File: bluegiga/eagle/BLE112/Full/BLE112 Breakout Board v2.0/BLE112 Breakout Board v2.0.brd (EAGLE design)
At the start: 38.1 x 22.9 mm, 27 parts, among them U1 BLE112-A, U2 MCP1700

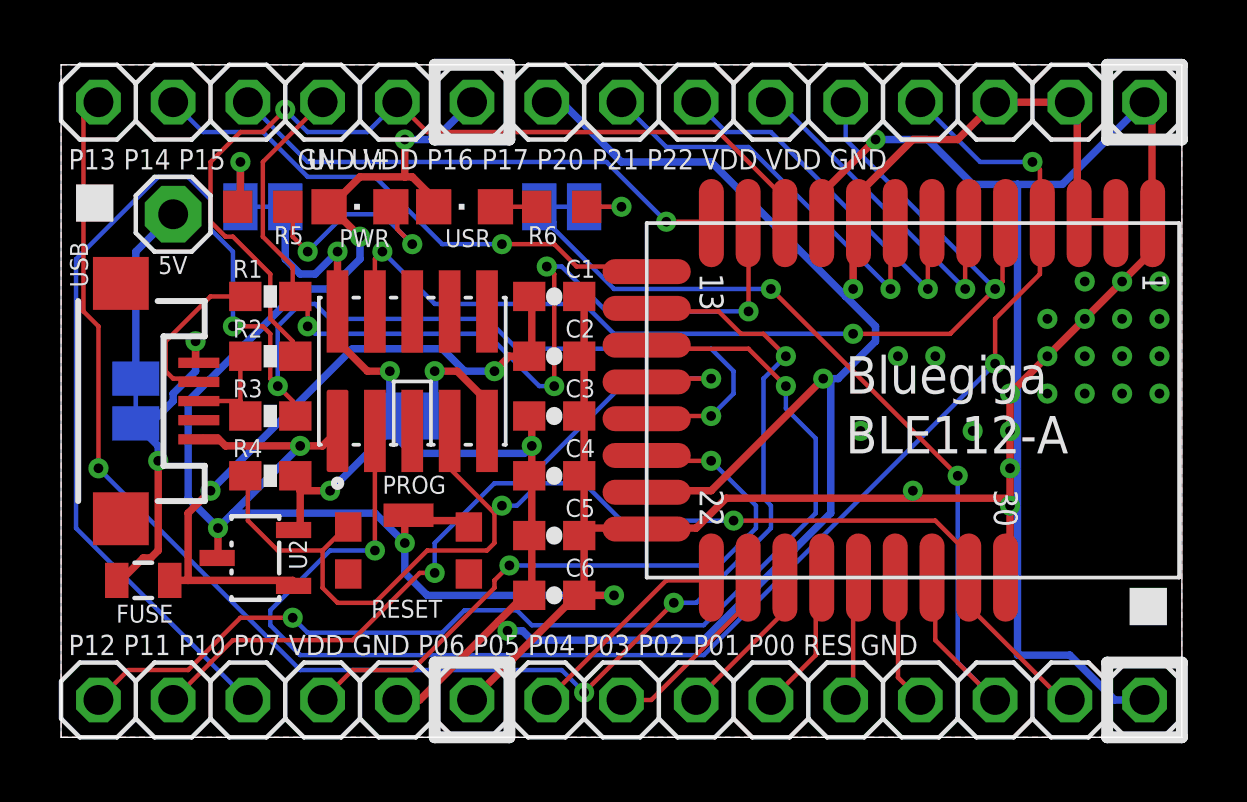
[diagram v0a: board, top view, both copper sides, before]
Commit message: Fix BLE112 v2.0 trial run PCB error
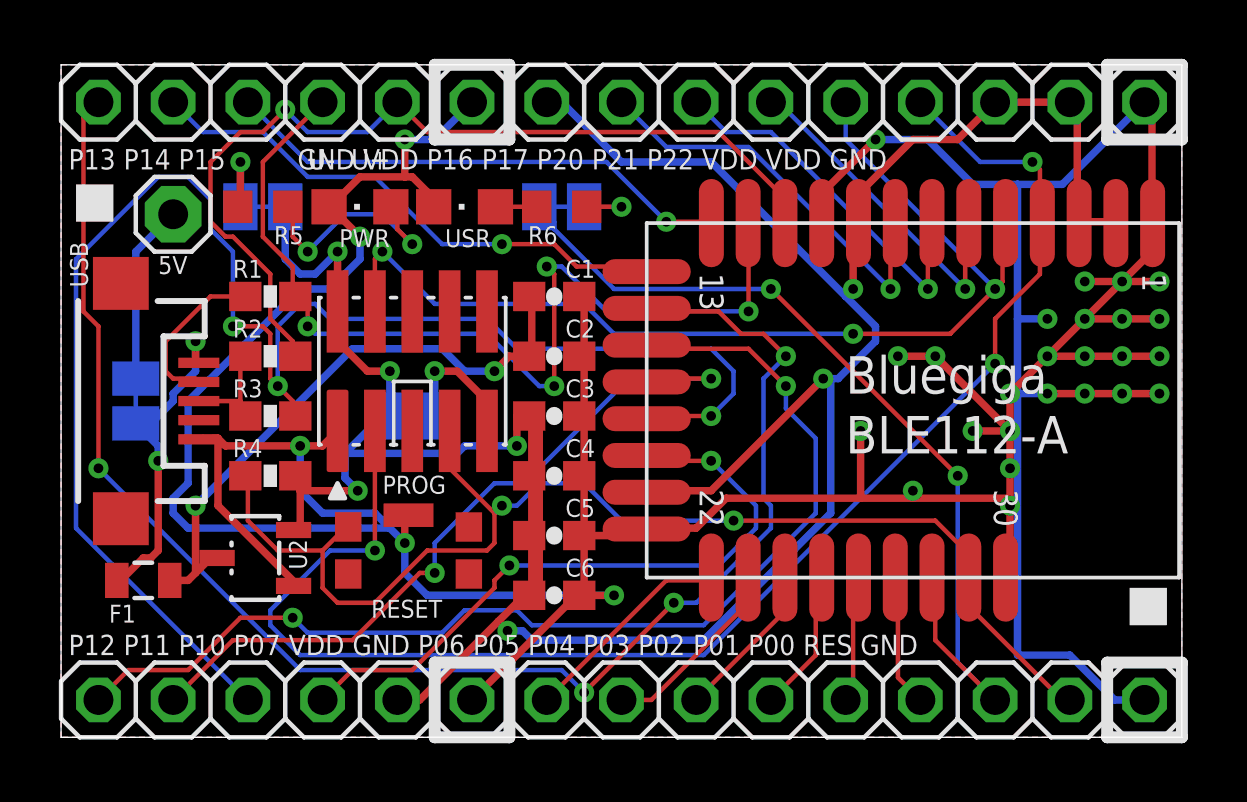
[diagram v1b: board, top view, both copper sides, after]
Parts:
- renumbered FUSE to F1
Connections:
- net 5V: now also U2.3; no longer U2.1
- net GND: now also S1.2, U2.1; no longer S1.3, U2.3
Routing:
- net GND: track 137.9 -> 167.0 mm, vias 31 -> 30
- net 3.3V: track 95.4 -> 105.5 mm
- net 5V: track 23.3 -> 20.5 mm
